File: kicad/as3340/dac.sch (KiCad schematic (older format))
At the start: 20 parts, among them U12 TL074, U13 LM4040AIM3-5.0, U14 TLV5610IDW

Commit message: start revision 0.3 of board
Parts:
- removed TP1: TestPoint, TestPoint:TestPoint_Pad_2.0x2.0mm, symbol Connector:TestPoint
- R61: LCSC Part C25804 -> (none)
- R64: value 20k -> 15k; LCSC Part C4184 -> (none)
- U13: value LM4040AIM3-5.0 -> LM4040AIM3-2.5; footprint Package_TO_SOT_THT:TO-92L_Inline -> Package_TO_SOT_THT:TO-92_Inline_Wide
- U14: symbol as3340-rescue:TLV5610IDW-Audio -> Audio:TLV5610IDW
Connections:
- wire segments 91 -> 89
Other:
- note added: "DAC Output Levels:\n\nFREQ_CV_DAC: 0 : 10V\nLINEAR_FM_DAC: +/- 5V\nEXT_OSC_VCA_AMOUNT: 0 : 2V\nPULSE_VCA_AMOUNT_DAC: 0 : 2V\nPWM_DAC: 0 : -4V (inverted to positive downstream)\nSYNC_LEVEL_DAC: 0 : 5V (no buffering)"
- note removed: "DAC Output Levels:\n\nFREQ_CV_DAC: 0 : 10V\nLINEAR_FM_DAC: +/- 5V\nEXT_OSC_VCA_AMOUNT: 0 : 2V\nPULSE_VCA_AMOUNT_DAC: 0 : 2V\nPWM_DAC: 0 : -5V (inverted to positive downstream)\nSYNC_LEVEL_DAC: 0 : 5V (no buffering)"
- moved on the sheet: C16, C24, C25, C5, R47, R48, R49, R50, R51, R52, R53, R54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

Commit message: routed v0.3
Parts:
- added R63, R68, R69: R, Resistor_SMD:R_0603_1608Metric, symbol Device:R
- added unit 4 of U12
- R52, R53: value 30k -> 8k2; LCSC Part C22984 -> (none)
- R54, R55: value 20k -> 33k; LCSC Part C4184 -> (none)
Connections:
- net GND: now also R68.2
- net SYNC_LEVEL_DAC: now also R69.1, U12.14; no longer U14.13 (OUTB)
- net VREF_2.5V: now also R63.2
- new net: R63.1, R68.1, R69.2, U12.13 (-)
- new net SYNC_LEVEL_FROM_DAC: U12.12 (+), U14.13 (OUTB)
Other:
- note added: "PWM: 0 : -3.75V"
- note added: "Sync Phase: TODO -2.5 : 5V ???"
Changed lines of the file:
@@
 	0    1    1    0
 $EndComp
-Text HLabel 6000 2500 2    50   Output ~ 0
-SYNC_LEVEL_DAC
 Text HLabel 5400 5750 2    50   Output ~ 0
 FREQ_CV_DAC
@@
 Text Label 4950 3100 0    50   ~ 0
 LINEAR_FM_FROM_DAC
-Text Label 4950 2500 0    50   ~ 0
+Text Label 5800 2500 2    50   ~ 0
 SYNC_LEVEL_FROM_DAC
 Wire Wire Line
@@
 AR Path="/61FF2290/64F3F53D" Ref="R52"  Part="1"
 F 0 "R52" V 9900 4600 50  0000 C CNN
-F 1 "30k" V 9700 4600 50  0000 C CNN
+F 1 "8k2" V 9700 4600 50  0000 C CNN
 F 2 "Resistor_SMD:R_0603_1608Metric" V 9730 4600 50  0001 C CNN
 F 3 "~" H 9800 4600 50  0001 C CNN
-F 4 "C22984" H 9800 4600 50  0001 C CNN "LCSC Part"
+F 4 "" H 9800 4600 50  0001 C CNN "LCSC Part"
 	1    9800 4600
 	0    1    1    0
@@
 AR Path="/61FF2290/64F40487" Ref="R54"  Part="1"
 F 0 "R54" V 10250 4850 50  0000 C CNN
-F 1 "20k" V 10050 4850 50  0000 C CNN
+F 1 "33k" V 10050 4850 50  0000 C CNN
 F 2 "Resistor_SMD:R_0603_1608Metric" V 10080 4850 50  0001 C CNN
 F 3 "~" H 10150 4850 50  0001 C CNN
-F 4 "C4184" H 10150 4850 50  0001 C CNN "LCSC Part"
+F 4 "" H 10150 4850 50  0001 C CNN "LCSC Part"
 	1    10150 4850
 	-1   0    0    1
@@
 AR Path="/61FF2290/64F72033" Ref="R53"  Part="1"
 F 0 "R53" V 9900 6000 50  0000 C CNN
-F 1 "30k" V 9700 6000 50  0000 C CNN
+F 1 "8k2" V 9700 6000 50  0000 C CNN
 F 2 "Resistor_SMD:R_0603_1608Metric" V 9730 6000 50  0001 C CNN
 F 3 "~" H 9800 6000 50  0001 C CNN
-F 4 "C22984" H 9800 6000 50  0001 C CNN "LCSC Part"
+F 4 "" H 9800 6000 50  0001 C CNN "LCSC Part"
 	1    9800 6000
 	0    1    1    0
@@
 AR Path="/61FF2290/64F7203E" Ref="R55"  Part="1"
 F 0 "R55" V 10250 6250 50  0000 C CNN
-F 1 "20k" V 10050 6250 50  0000 C CNN
+F 1 "33k" V 10050 6250 50  0000 C CNN
 F 2 "Resistor_SMD:R_0603_1608Metric" V 10080 6250 50  0001 C CNN
 F 3 "~" H 10150 6250 50  0001 C CNN
-F 4 "C4184" H 10150 6250 50  0001 C CNN "LCSC Part"
+F 4 "" H 10150 6250 50  0001 C CNN "LCSC Part"
 	1    10150 6250
 	-1   0    0    1
@@
 Wire Wire Line
 	4700 7400 4950 7400
-Wire Wire Line
-	4850 2500 6000 2500
 Wire Wire Line
 	10150 4600 10450 4600
@@
 Wire Notes Line
 	8300 1700 11350 1700
+Text HLabel 14350 2200 2    50   Output ~ 0
+SYNC_LEVEL_DAC
+$Comp
+L Amplifier_Operational:TL074 U?
+U 4 1 62E91106
+P 13750 2200
+AR Path="/61BB3C36/62E91106" Ref="U?"  Part="4"
+AR Path="/61FF2290/62E91106" Ref="U12"  Part="4"
+F 0 "U12" H 13850 2350 50  0000 C CNN
+F 1 "TL074" H 13700 2200 50  0000 C CNN
+F 2 "Package_SO:SOIC-14_3.9x8.7mm_P1.27mm" H 13700 2300 50  0001 C CNN
+F 3 "http://www.ti.com/lit/ds/symlink/tl071.pdf" H 13800 2400 50  0001 C CNN
+F 4 "C12594" H 13750 2200 50  0001 C CNN "LCSC Part"
+	4    13750 2200
+	1    0    0    1
+$EndComp
+Wire Wire Line
+	14050 2200 14150 2200
+Text Label 12050 1750 0    50   ~ 0
+VREF_2.5V
+Wire Wire Line
+	12500 1750 12050 1750
+$Comp
+L power:GND #PWR0131
+U 1 1 62E91116
+P 12250 2200
+F 0 "#PWR0131" H 12250 1950 50  0001 C CNN
+F 1 "GND" H 12255 2027 50  0000 C CNN
+F 2 "" H 12250 2200 50  0001 C CNN
+F 3 "" H 12250 2200 50  0001 C CNN
+	1    12250 2200
+	1    0    0    -1
+$EndComp
+Wire Wire Line
+	12250 2100 12500 2100
+Wire Wire Line
+	12800 2100 13250 2100
+Wire Wire Line
+	12800 1750 13250 1750
+Wire Wire Line
+	13250 1750 13250 2100
+Connection ~ 13250 1750
+Wire Wire Line
+	13250 1750 13550 1750
+Connection ~ 13250 2100
+Wire Wire Line
+	13250 2100 13450 2100
+Wire Wire Line
+	13850 1750 14150 1750
+Wire Wire Line
+	14150 1750 14150 2200
+Connection ~ 14150 2200
+Wire Wire Line
+	13200 2300 13200 2800
+Wire Wire Line
+	13200 2300 13450 2300
+Wire Wire Line
+	12250 2100 12250 2200
+Wire Wire Line
+	12050 2800 13200 2800
+Wire Wire Line
+	14150 2200 14350 2200
+Wire Wire Line
+	4850 2500 5800 2500
+Text Label 12050 2800 0    50   ~ 0
+SYNC_LEVEL_FROM_DAC
+Text Notes 11900 1500 0    50   ~ 0
+Sync Phase: TODO -2.5 : 5V ???
+Wire Notes Line
+	11800 1400 15100 1400
+Wire Notes Line
+	15100 1400 15100 2900
+Wire Notes Line
+	15100 2900 11800 2900
+Wire Notes Line
+	11800 2900 11800 1400
+Text Notes 8550 1850 0    50   ~ 0
+PWM: 0 : -3.75V
+$Comp
+L Device:R R69
+U 1 1 631A62A0
+P 13700 1750
+F 0 "R69" V 13493 1750 50  0000 C CNN
+F 1 "R" V 13584 1750 50  0000 C CNN
+F 2 "Resistor_SMD:R_0603_1608Metric" V 13630 1750 50  0001 C CNN
+F 3 "~" H 13700 1750 50  0001 C CNN
+	1    13700 1750
+	0    1    1    0
+$EndComp
+$Comp
+L Device:R R63
+U 1 1 631A6C09
+P 12650 1750
+F 0 "R63" V 12443 1750 50  0000 C CNN
+F 1 "R" V 12534 1750 50  0000 C CNN
+F 2 "Resistor_SMD:R_0603_1608Metric" V 12580 1750 50  0001 C CNN
+F 3 "~" H 12650 1750 50  0001 C CNN
+	1    12650 1750
+	0    1    1    0
+$EndComp
+$Comp
+L Device:R R68
+U 1 1 631A7238
+P 12650 2100
+F 0 "R68" V 12443 2100 50  0000 C CNN
+F 1 "R" V 12534 2100 50  0000 C CNN
+F 2 "Resistor_SMD:R_0603_1608Metric" V 12580 2100 50  0001 C CNN
+F 3 "~" H 12650 2100 50  0001 C CNN
+	1    12650 2100
+	0    1    1    0
+$EndComp
 $EndSCHEMATC

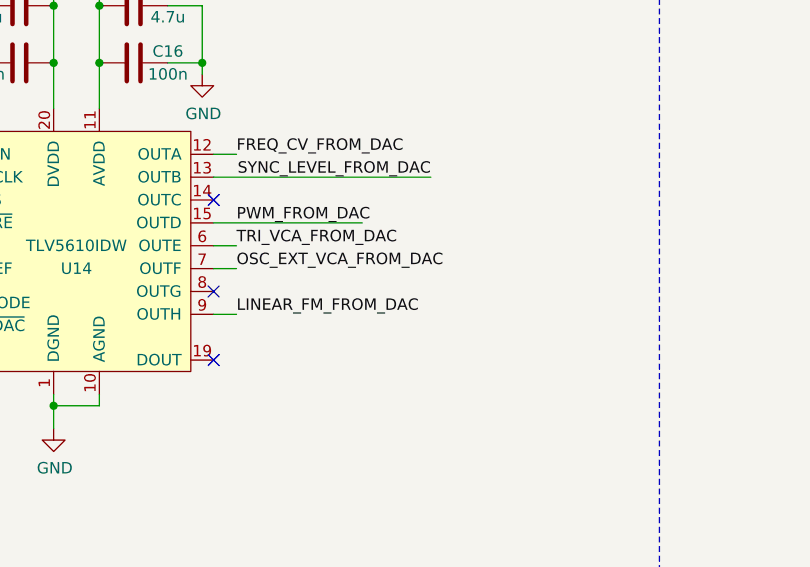
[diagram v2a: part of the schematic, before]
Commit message: added id chip and some tweaks
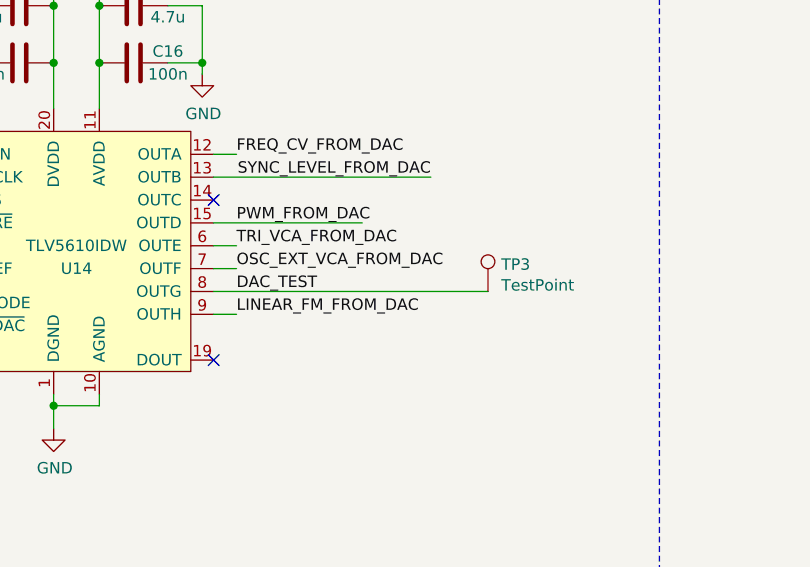
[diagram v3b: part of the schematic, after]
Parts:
- added TP3: TestPoint, TestPoint:TestPoint_Pad_2.0x2.0mm, symbol Connector:TestPoint
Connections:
- net DAC_TEST: now reaches U14.8 (OUTG)
- net DAC_TEST: now also TP3.1
- no-connect marks 3 -> 2
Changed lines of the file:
@@
 Text Label 5800 2500 2    50   ~ 0
 SYNC_LEVEL_FROM_DAC
-Wire Wire Line
-	4850 3100 4950 3100
 Text Label 4950 2900 0    50   ~ 0
 OSC_EXT_VCA_FROM_DAC
@@
 	4150 3500 4150 3600
 Connection ~ 4150 2000
-NoConn ~ 4850 3000
 NoConn ~ 4850 2600
 NoConn ~ 4850 3300
@@
 	0    1    1    0
 $EndComp
+$Comp
+L Connector:TestPoint TP3
+U 1 1 62D121B0
+P 6050 3000
+F 0 "TP3" H 6108 3118 50  0000 L CNN
+F 1 "TestPoint" H 6108 3027 50  0000 L CNN
+F 2 "TestPoint:TestPoint_Pad_2.0x2.0mm" H 6250 3000 50  0001 C CNN
+F 3 "~" H 6250 3000 50  0001 C CNN
+F 4 "952-2664-6-ND" H 6050 3000 50  0001 C CNN "Digikey"
+	1    6050 3000
+	1    0    0    -1
+$EndComp
+Wire Wire Line
+	4950 3100 4850 3100
+Wire Wire Line
+	4850 3000 6050 3000
+Text Label 4950 3000 0    50   ~ 0
+DAC_TEST
 $EndSCHEMATC

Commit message: routed for v0.3 -- perhaps final
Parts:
- removed R63: R, Resistor_SMD:R_0603_1608Metric, symbol Device:R
- added C39: 100n, Capacitor_SMD:C_0603_1608Metric, symbol Device:C
- R68: value R -> 10k
- R69: value R -> 30k
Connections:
- net GND: now also C39.2
- net VREF_2.5V: now also C39.1
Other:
- note added: "DAC Output Levels:\n\nFREQ_CV_DAC: 0 : 10V\nLINEAR_FM_DAC: +/- 5V\nEXT_OSC_VCA_AMOUNT: 0 : 2V\nPULSE_VCA_AMOUNT_DAC: 0 : 2V\nPWM_DAC: 0 : -3.75V (inverted to positive downstream)\nSYNC_LEVEL_DAC: 0 : 10V (sync phase)"
- note added: "Sync Phase: 0 : 10V"
- note removed: "DAC Output Levels:\n\nFREQ_CV_DAC: 0 : 10V\nLINEAR_FM_DAC: +/- 5V\nEXT_OSC_VCA_AMOUNT: 0 : 2V\nPULSE_VCA_AMOUNT_DAC: 0 : 2V\nPWM_DAC: 0 : -4V (inverted to positive downstream)\nSYNC_LEVEL_DAC: 0 : 5V (no buffering)"
- note removed: "Sync Phase: TODO -2.5 : 5V ???"
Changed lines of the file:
@@
 	4850 2700 5500 2700
 Wire Notes Line
-	2350 1300 6800 1300
+	1800 1300 6800 1300
 Wire Notes Line
 	6800 1300 6800 4300
 Wire Notes Line
-	6800 4300 2350 4300
-Wire Notes Line
-	2350 4300 2350 1300
+	6800 4300 1800 4300
+Wire Notes Line
+	1800 4300 1800 1300
 Text Notes 8250 7900 0    50   ~ 0
-DAC Output Levels:\n\nFREQ_CV_DAC:  0 : 10V\nLINEAR_FM_DAC: +/- 5V\nEXT_OSC_VCA_AMOUNT: 0 : 2V\nPULSE_VCA_AMOUNT_DAC: 0 : 2V\nPWM_DAC: 0 : -4V (inverted to positive downstream)\nSYNC_LEVEL_DAC: 0 : 5V (no buffering)
+DAC Output Levels:\n\nFREQ_CV_DAC:  0 : 10V\nLINEAR_FM_DAC: +/- 5V\nEXT_OSC_VCA_AMOUNT: 0 : 2V\nPULSE_VCA_AMOUNT_DAC: 0 : 2V\nPWM_DAC: 0 : -3.75V (inverted to positive downstream)\nSYNC_LEVEL_DAC: 0 : 10V (sync phase)
 $Comp
 L Device:R R?
@@
 Wire Wire Line
 	14050 2200 14150 2200
-Text Label 12050 1750 0    50   ~ 0
-VREF_2.5V
-Wire Wire Line
-	12500 1750 12050 1750
 $Comp
 L power:GND #PWR0131
@@
 	12800 2100 13250 2100
 Wire Wire Line
-	12800 1750 13250 1750
-Wire Wire Line
 	13250 1750 13250 2100
-Connection ~ 13250 1750
 Wire Wire Line
 	13250 1750 13550 1750
@@
 SYNC_LEVEL_FROM_DAC
 Text Notes 11900 1500 0    50   ~ 0
-Sync Phase: TODO -2.5 : 5V ???
+Sync Phase: 0 : 10V
 Wire Notes Line
 	11800 1400 15100 1400
@@
 P 13700 1750
 F 0 "R69" V 13493 1750 50  0000 C CNN
-F 1 "R" V 13584 1750 50  0000 C CNN
+F 1 "30k" V 13584 1750 50  0000 C CNN
 F 2 "Resistor_SMD:R_0603_1608Metric" V 13630 1750 50  0001 C CNN
 F 3 "~" H 13700 1750 50  0001 C CNN
@@
 $EndComp
 $Comp
-L Device:R R63
-U 1 1 631A6C09
-P 12650 1750
-F 0 "R63" V 12443 1750 50  0000 C CNN
-F 1 "R" V 12534 1750 50  0000 C CNN
-F 2 "Resistor_SMD:R_0603_1608Metric" V 12580 1750 50  0001 C CNN
-F 3 "~" H 12650 1750 50  0001 C CNN
-	1    12650 1750
-	0    1    1    0
-$EndComp
-$Comp
 L Device:R R68
 U 1 1 631A7238
 P 12650 2100
 F 0 "R68" V 12443 2100 50  0000 C CNN
-F 1 "R" V 12534 2100 50  0000 C CNN
+F 1 "10k" V 12534 2100 50  0000 C CNN
 F 2 "Resistor_SMD:R_0603_1608Metric" V 12580 2100 50  0001 C CNN
 F 3 "~" H 12650 2100 50  0001 C CNN
@@
 Text Label 4950 3000 0    50   ~ 0
 DAC_TEST
+$Comp
+L Device:C C39
+U 1 1 63892908
+P 2200 3100
+F 0 "C39" V 2250 2950 50  0000 C CNN
+F 1 "100n" V 2150 2950 50  0000 C CNN
+F 2 "Capacitor_SMD:C_0603_1608Metric" H 2238 2950 50  0001 C CNN
+F 3 "~" H 2200 3100 50  0001 C CNN
+F 4 "C14663" V 2200 3100 50  0001 C CNN "LCSC"
+F 5 "C14663" H 2200 3100 50  0001 C CNN "LCSC Part"
+	1    2200 3100
+	1    0    0    -1
+$EndComp
+Wire Wire Line
+	2200 2950 2650 2950
+Connection ~ 2650 2950
+Wire Wire Line
+	2200 3250 2200 3350
+Wire Wire Line
+	2200 3350 2650 3350
+Connection ~ 2650 3350
 $EndSCHEMATC

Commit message: update gerber files and assembly
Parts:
- C16, C25, C39: value 100n -> 0.1u
- R52, R53: LCSC Part (none) -> C25981
- R54, R55: LCSC Part (none) -> C4216
- R61, R68: LCSC Part (none) -> C25804
- R64: LCSC Part (none) -> C22809
- R69: LCSC Part (none) -> C22984
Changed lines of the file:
@@
 P 4000 2000
 F 0 "C25" V 4050 2150 50  0000 C CNN
-F 1 "100n" V 3950 2150 50  0000 C CNN
+F 1 "0.1u" V 3950 2150 50  0000 C CNN
 F 2 "Capacitor_SMD:C_0603_1608Metric" H 4038 1850 50  0001 C CNN
 F 3 "~" H 4000 2000 50  0001 C CNN
@@
 F 2 "Resistor_SMD:R_0603_1608Metric" V 9730 4600 50  0001 C CNN
 F 3 "~" H 9800 4600 50  0001 C CNN
-F 4 "" H 9800 4600 50  0001 C CNN "LCSC Part"
+F 4 "C25981" H 9800 4600 50  0001 C CNN "LCSC Part"
 	1    9800 4600
 	0    1    1    0
@@
 F 2 "Resistor_SMD:R_0603_1608Metric" V 10080 4850 50  0001 C CNN
 F 3 "~" H 10150 4850 50  0001 C CNN
-F 4 "" H 10150 4850 50  0001 C CNN "LCSC Part"
+F 4 "C4216" H 10150 4850 50  0001 C CNN "LCSC Part"
 	1    10150 4850
 	-1   0    0    1
@@
 F 2 "Resistor_SMD:R_0603_1608Metric" V 9730 6000 50  0001 C CNN
 F 3 "~" H 9800 6000 50  0001 C CNN
-F 4 "" H 9800 6000 50  0001 C CNN "LCSC Part"
+F 4 "C25981" H 9800 6000 50  0001 C CNN "LCSC Part"
 	1    9800 6000
 	0    1    1    0
@@
 F 2 "Resistor_SMD:R_0603_1608Metric" V 10080 6250 50  0001 C CNN
 F 3 "~" H 10150 6250 50  0001 C CNN
-F 4 "" H 10150 6250 50  0001 C CNN "LCSC Part"
+F 4 "C4216" H 10150 6250 50  0001 C CNN "LCSC Part"
 	1    10150 6250
 	-1   0    0    1
@@
 P 4500 2000
 F 0 "C16" V 4550 1850 50  0000 C CNN
-F 1 "100n" V 4450 1850 50  0000 C CNN
+F 1 "0.1u" V 4450 1850 50  0000 C CNN
 F 2 "Capacitor_SMD:C_0603_1608Metric" H 4538 1850 50  0001 C CNN
 F 3 "~" H 4500 2000 50  0001 C CNN
@@
 F 2 "Resistor_SMD:R_0603_1608Metric" V 10230 2050 50  0001 C CNN
 F 3 "~" H 10300 2050 50  0001 C CNN
-F 4 "" H 10300 2050 50  0001 C CNN "LCSC Part"
+F 4 "C22809" H 10300 2050 50  0001 C CNN "LCSC Part"
 	1    10300 2050
 	0    1    1    0
@@
 F 2 "Resistor_SMD:R_0603_1608Metric" V 9580 2300 50  0001 C CNN
 F 3 "~" H 9650 2300 50  0001 C CNN
-F 4 "" H 9650 2300 50  0001 C CNN "LCSC Part"
+F 4 "C25804" H 9650 2300 50  0001 C CNN "LCSC Part"
 	1    9650 2300
 	0    1    1    0
@@
 F 2 "Resistor_SMD:R_0603_1608Metric" V 13630 1750 50  0001 C CNN
 F 3 "~" H 13700 1750 50  0001 C CNN
+F 4 "C22984" H 13700 1750 50  0001 C CNN "LCSC Part"
 	1    13700 1750
 	0    1    1    0
@@
 F 2 "Resistor_SMD:R_0603_1608Metric" V 12580 2100 50  0001 C CNN
 F 3 "~" H 12650 2100 50  0001 C CNN
+F 4 "C25804" H 12650 2100 50  0001 C CNN "LCSC Part"
 	1    12650 2100
 	0    1    1    0
@@
 P 2200 3100
 F 0 "C39" V 2250 2950 50  0000 C CNN
-F 1 "100n" V 2150 2950 50  0000 C CNN
+F 1 "0.1u" V 2150 2950 50  0000 C CNN
 F 2 "Capacitor_SMD:C_0603_1608Metric" H 2238 2950 50  0001 C CNN
 F 3 "~" H 2200 3100 50  0001 C CNN
